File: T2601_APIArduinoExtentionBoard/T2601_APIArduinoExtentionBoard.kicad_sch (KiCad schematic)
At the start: 93 parts, among them J1 Conn_01x10_Socket, J11 Conn_01x04_Pin, J12 Screw_Terminal_01x02, J13 Conn_01x04_Pin, J14 Screw_Terminal_01x02, J15 Conn_02x08_Counter_Clockwise, J2 Conn_01x10_Socket, J3 Conn_01x10_Socket, J4 Conn_01x10_Socket, J5 Screw_Terminal_01x08, J6 Screw_Terminal_01x08, J7 Conn_02x03_Counter_Clockwise, J8 Conn_01x04, J9 Conn_02x08_Counter_Clockwise, U1 ATMEGA328P-AU, X1 X322516MOB4SI

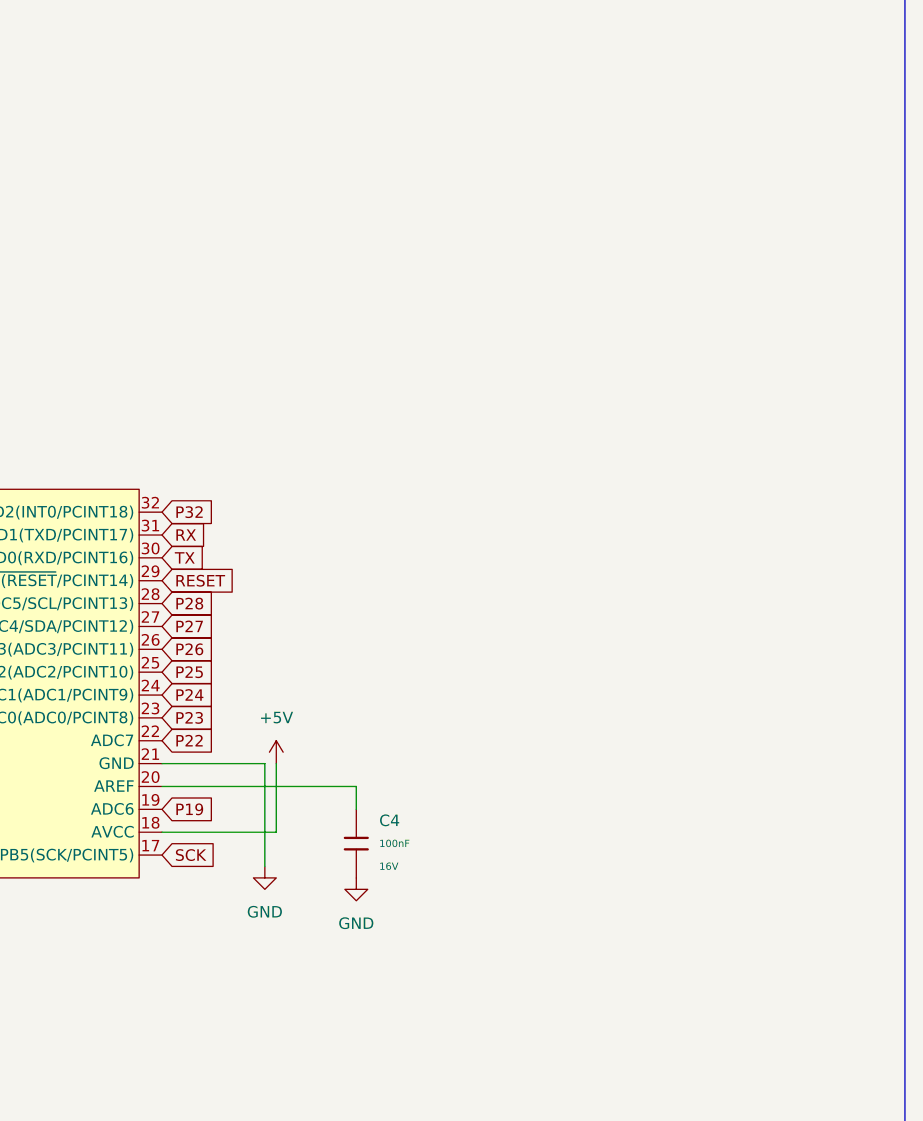
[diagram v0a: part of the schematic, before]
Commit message: switch to atmega328PB
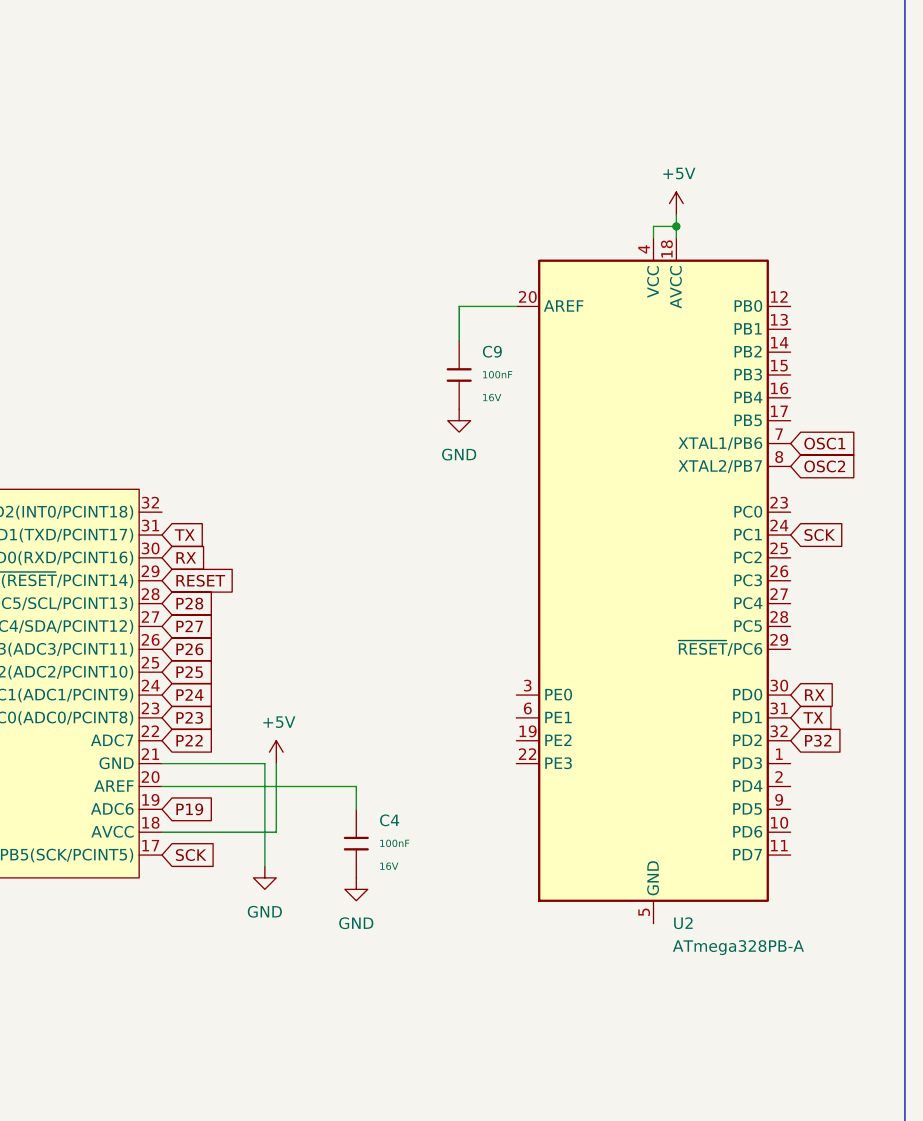
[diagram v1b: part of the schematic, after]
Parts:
- added C9: 100nF, PCM_JLCPCB:C_0402, symbol PCM_JLCPCB-Capacitors:0402,100nF
- added U2: ATmega328PB-A, Package_QFP:TQFP-32_7x7mm_P0.8mm, symbol MCU_Microchip_ATmega:ATmega328PB-A
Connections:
- net +5V: now also U2.18 (AVCC), U2.4 (VCC)
- net GND: now also C9.2
- net OSC1: now also U2.7 (XTAL1/PB6)
- net OSC2: now also U2.8 (XTAL2/PB7)
- net P32: now also U2.32 (PD2); no longer U1.32 (PD2(INT0/PCINT18))
- net RX: now also U1.30 (PD0(RXD/PCINT16)), U2.30 (PD0); no longer U1.31 (PD1(TXD/PCINT17))
- net SCK: now also U2.24 (PC1)
- net TX: now also U1.31 (PD1(TXD/PCINT17)), U2.31 (PD1); no longer U1.30 (PD0(RXD/PCINT16))
- new net: C9.1, U2.20 (AREF)
- new net: U2.21 (GND), U2.5 (GND)

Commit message: kicad modif
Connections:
- net MISO: now also U2.23 (PC0)
- net MOSI: now also U2.22 (PE3)
- net P1: now also U2.1 (PD3)
- net P2: now also U2.2 (PD4)
- net RESET: now also U2.29 (~{RESET}/PC6); no longer U1.29 (~{PC6(RESET}/PCINT14))
- net RX: no longer U1.30 (PD0(RXD/PCINT16))
- net TX: no longer U1.31 (PD1(TXD/PCINT17))
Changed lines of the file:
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@@
+		)
+	)
+	(global_label "P25"
+		(shape input)
+		(at 365.76 294.64 0)
+		(fields_autoplaced yes)
+		(effects
+			(font
+				(size 1.27 1.27)
+			)
+			(justify left)
+		)
+		(property "Intersheetrefs" "${INTERSHEET_REFS}"
+			(at 372.4342 294.64 0)
+			(hide yes)
+			(show_name no)
+			(do_not_autoplace no)
+			(effects
+				(font
+					(size 1.27 1.27)
+				)
+				(justify left)
+			)
 		)
 	)
@@
 		)
 	)
+	(global_label "MOSI"
+		(shape input)
+		(at 306.07 317.5 180)
+		(fields_autoplaced yes)
+		(effects
+			(font
+				(size 1.27 1.27)
+			)
+			(justify right)
+		)
+		(property "Intersheetrefs" "${INTERSHEET_REFS}"
+			(at 298.4886 317.5 0)
+			(hide yes)
+			(show_name no)
+			(do_not_autoplace no)
+			(effects
+				(font
+					(size 1.27 1.27)
+				)
+				(justify right)
+			)
+		)
+	)
 	(global_label "P12"
 		(shape input)
@@
 		)
 	)
+	(global_label "P27"
+		(shape input)
+		(at 365.76 299.72 0)
+		(fields_autoplaced yes)
+		(effects
+			(font
+				(size 1.27 1.27)
+			)
+			(justify left)
+		)
+		(property "Intersheetrefs" "${INTERSHEET_REFS}"
+			(at 372.4342 299.72 0)
+			(hide yes)
+			(show_name no)
+			(do_not_autoplace no)
+			(effects
+				(font
+					(size 1.27 1.27)
+				)
+				(justify left)
+			)
+		)
+	)
 	(global_label "TX_DEBUG"
 		(shape input)
@@
 	(global_label "RESET"
 		(shape input)
-		(at 266.7 297.18 0)
-		(fields_autoplaced yes)
-		(effects
-			(font
-				(size 1.27 1.27)
-			)
-			(justify left)
-		)
-		(property "Intersheetrefs" "${INTERSHEET_REFS}"
-			(at 275.4303 297.18 0)
+		(at 336.55 304.8 0)
+		(fields_autoplaced yes)
+		(effects
+			(font
+				(size 1.27 1.27)
+			)
+			(justify left)
+		)
+		(property "Intersheetrefs" "${INTERSHEET_REFS}"
+			(at 345.2803 304.8 0)
 			(hide yes)
 			(show_name no)
@@
 		)
 	)
+	(global_label "MISO"
+		(shape input)
+		(at 336.55 289.56 0)
+		(fields_autoplaced yes)
+		(effects
+			(font
+				(size 1.27 1.27)
+			)
+			(justify left)
+		)
+		(property "Intersheetrefs" "${INTERSHEET_REFS}"
+			(at 344.1314 289.56 0)
+			(hide yes)
+			(show_name no)
+			(do_not_autoplace no)
+			(effects
+				(font
+					(size 1.27 1.27)
+				)
+				(justify left)
+			)
+		)
+	)
 	(global_label "P1"
 		(shape input)
@@
 		)
 	)
+	(global_label "P1"
+		(shape input)
+		(at 336.55 317.5 0)
+		(fields_autoplaced yes)
+		(effects
+			(font
+				(size 1.27 1.27)
+			)
+			(justify left)
+		)
+		(property "Intersheetrefs" "${INTERSHEET_REFS}"
+			(at 342.0147 317.5 0)
+			(hide yes)
+			(show_name no)
+			(do_not_autoplace no)
+			(effects
+				(font
+					(size 1.27 1.27)
+				)
+				(justify left)
+			)
+		)
+	)
 	(global_label "P13"
 		(shape input)
@@
 		)
 	)
+	(global_label "P2"
+		(shape input)
+		(at 336.55 320.04 0)
+		(fields_autoplaced yes)
+		(effects
+			(font
+				(size 1.27 1.27)
+			)
+			(justify left)
+		)
+		(property "Intersheetrefs" "${INTERSHEET_REFS}"
+			(at 342.0147 320.04 0)
+			(hide yes)
+			(show_name no)
+			(do_not_autoplace no)
+			(effects
+				(font
+					(size 1.27 1.27)
+				)
+				(justify left)
+			)
+		)
+	)
+	(global_label "P28"
+		(shape input)
+		(at 365.76 302.26 0)
+		(fields_autoplaced yes)
+		(effects
+			(font
+				(size 1.27 1.27)
+			)
+			(justify left)
+		)
+		(property "Intersheetrefs" "${INTERSHEET_REFS}"
+			(at 372.4342 302.26 0)
+			(hide yes)
+			(show_name no)
+			(do_not_autoplace no)
+			(effects
+				(font
+					(size 1.27 1.27)
+				)
+				(justify left)
+			)
+		)
+	)
 	(global_label "P14"
 		(shape input)
@@
 		)
 	)
-	(global_label "TX"
-		(shape input)
-		(at 266.7 292.1 0)
-		(fields_autoplaced yes)
-		(effects
-			(font
-				(size 1.27 1.27)
-			)
-			(justify left)
-		)
-		(property "Intersheetrefs" "${INTERSHEET_REFS}"
-			(at 271.8623 292.1 0)
-			(hide yes)
-			(show_name no)
-			(do_not_autoplace no)
-			(effects
-				(font
-					(size 1.27 1.27)
-				)
-				(justify left)
-			)
-		)
-	)
 	(global_label "P11"
 		(shape input)
@@
 		)
 	)
+	(global_label "P26"
+		(shape input)
+		(at 365.76 297.18 0)
+		(fields_autoplaced yes)
+		(effects
+			(font
+				(size 1.27 1.27)
+			)
+			(justify left)
+		)
+		(property "Intersheetrefs" "${INTERSHEET_REFS}"
+			(at 372.4342 297.18 0)
+			(hide yes)
+			(show_name no)
+			(do_not_autoplace no)
+			(effects
+				(font
+					(size 1.27 1.27)
+				)
+				(justify left)
+			)
+		)
+	)
 	(global_label "MISO"
 		(shape input)
@@
 			(hide yes)
 			(show_name no)
-			(do_not_autoplace no)
-			(effects
-				(font
-					(size 1.27 1.27)
-				)
-				(justify left)
-			)
-		)
-	)
-	(global_label "RX"
-		(shape input)
-		(at 266.7 294.64 0)
-		(fields_autoplaced yes)
-		(effects
-			(font
-				(size 1.27 1.27)
-			)
-			(justify left)
-		)
-		(property "Intersheetrefs" "${INTERSHEET_REFS}"
-			(at 272.1647 294.64 0)
-			(hide yes)
-			(show_name no)

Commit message: Kicad Modification, switch ATMEGA328P to ATMEGA328PB, schematic modification + rerouting, V0 version, no verification
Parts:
- removed C4: 100nF, PCM_JLCPCB:C_0402, symbol PCM_JLCPCB-Capacitors:0402,100nF
- removed D13: Red, PCM_JLCPCB:D_0805, symbol PCM_JLCPCB-Diodes:LED,0805,Red
- removed R2: 1kΩ, PCM_JLCPCB:R_0402, symbol PCM_JLCPCB-Resistors:0402,1kΩ
- removed U1: ATMEGA328P-AU, T2601_APIArduinoExtentionBoard_Lib:TQFP-32_L7.0-W7.0-P0.80-LS9.0-BL, symbol T2601_APIArduinoExtentionBoard_Lib:ATMEGA328P-AU
- added D27: Red, PCM_JLCPCB:D_0805, symbol PCM_JLCPCB-Diodes:LED,0805,Red
- added D28: Green, PCM_JLCPCB:D_0805, symbol PCM_JLCPCB-Diodes:LED,0805,Green
- added D29: Yellow, PCM_JLCPCB:D_0805, symbol PCM_JLCPCB-Diodes:LED,0805,Yellow
- added R26, R27, R28: 1kΩ, PCM_JLCPCB:R_0402, symbol PCM_JLCPCB-Resistors:0402,1kΩ
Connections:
- net GND: now also U2.21 (GND), U2.5 (GND), R26.2, R27.2, R28.2
- net MISO: now also U2.16 (PB4); no longer U2.23 (PC0)
- net MOSI: now also U2.15 (PB3); no longer U2.22 (PE3)
- net P10: now also J4.8 (Pin_8), R9.1, U2.10 (PD6); no longer J4.7 (Pin_7), R10.1
- net P11: now also J4.7 (Pin_7), R10.1, U2.11 (PD7); no longer J4.4 (Pin_4), R11.1
- net P12: now also J4.4 (Pin_4), R11.1, U2.12 (PB0); no longer J4.3 (Pin_3), R12.1
- net P13: now also J4.3 (Pin_3), R12.1, U2.13 (PB1); no longer J4.2 (Pin_2), R13.1
- net P14: now also J4.2 (Pin_2), R13.1, U2.14 (PB2); no longer J4.1 (Pin_1), R14.1
- net P19: now also U2.19 (PE2)
- net P2: now also J8.2 (Pin_2), D27.2; no longer J4.9 (Pin_9), R8.1
- net P22: now also U2.22 (PE3)
- net P23: now also U2.23 (PC0)
- net P24: now also U2.24 (PC1)
- net P25: now also U2.25 (PC2)
- net P26: now also U2.26 (PC3)
- net P27: now also U2.27 (PC4)
- net P28: now also U2.28 (PC5)
- net P32: now also J4.1 (Pin_1), R14.1; no longer J8.2 (Pin_2)
- net P9: now also J4.9 (Pin_9), R8.1, U2.9 (PD5); no longer J4.8 (Pin_8), R9.1
- net SCK: now also U2.17 (PB5); no longer U2.24 (PC1)
- net P3: now reaches U2.3 (PE0)
- net P3: now also D28.2
- net P6: now reaches U2.6 (PE1)
- net P6: now also D29.2
- new net: D29.1, R28.1
- new net: D28.1, R27.1
- new net: D27.1, R26.1
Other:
- note added: "State Indicator"
- note removed: "BLINK Indicator"
- moved on the sheet: C5, C6, C9, H1, H2, H3, H4, TP1, U2

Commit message: Modification Board to 4 layers, finition routing et re organisation des composants (leds statuts condo alim + reset
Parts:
- added TP2: TestPoint, TestPoint:TestPoint_Loop_D2.50mm_Drill1.0mm_LowProfile, symbol Connector:TestPoint
- TP1: footprint TestPoint:TestPoint_Pad_D2.0mm -> TestPoint:TestPoint_Loop_D2.50mm_Drill1.0mm_LowProfile
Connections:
- net RX: now also D12.2, TP2.1; no longer D11.2
- net TX: now also D11.2; no longer D12.2
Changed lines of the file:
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@@
 	(wire
 		(pts
+			(xy 39.37 190.5) (xy 38.1 190.5)
+		)
+		(stroke
+			(width 0)
+			(type default)
+		)
+	)
+	(wire
+		(pts
 			(xy 256.54 116.84) (xy 261.62 116.84)
 		)
@@
 	(wire
 		(pts
+			(xy 38.1 190.5) (xy 38.1 186.69)
+		)
+		(stroke
+			(width 0)
+			(type default)
+		)
+	)
+	(wire
+		(pts
 			(xy 262.89 41.91) (xy 262.89 40.64)
 		)
@@
 	(global_label "RX"
 		(shape input)
-		(at 24.13 69.85 90)
+		(at 34.29 69.85 90)
 		(fields_autoplaced yes)
 		(effects
@@
 		)
 		(property "Intersheetrefs" "${INTERSHEET_REFS}"
-			(at 24.13 64.3853 90)
+			(at 34.29 64.3853 90)
 			(hide yes)
 			(show_name no)
@@
 	(global_label "TX"
 		(shape input)
-		(at 34.29 69.85 90)
+		(at 24.13 69.85 90)
 		(fields_autoplaced yes)
 		(effects
@@
 		)
 		(property "Intersheetrefs" "${INTERSHEET_REFS}"
-			(at 34.29 64.6877 90)
+			(at 24.13 64.6877 90)
 			(hide yes)
 			(show_name no)
@@
 		)
 	)
+	(global_label "RX"
+		(shape input)
+		(at 39.37 190.5 0)
+		(fields_autoplaced yes)
+		(effects
+			(font
+				(size 1.27 1.27)
+			)
+			(justify left)
+		)
+		(property "Intersheetrefs" "${INTERSHEET_REFS}"
+			(at 44.8347 190.5 0)
+			(hide yes)
+			(show_name no)
+			(do_not_autoplace no)
+			(effects
+				(font
+					(size 1.27 1.27)
+				)
+				(justify left)
+			)
+		)
+	)
 	(global_label "P1"
 		(shape input)
@@
 	)
 	(symbol
+		(lib_id "Connector:TestPoint")
+		(at 38.1 186.69 0)
+		(unit 1)
+		(body_style 1)
+		(exclude_from_sim no)
+		(in_bom yes)
+		(on_board yes)
+		(in_pos_files yes)
+		(dnp no)
+		(fields_autoplaced yes)
+		(property "Reference" "TP2"
+			(at 40.64 182.1179 0)
+			(show_name no)
+			(do_not_autoplace no)
+			(effects
+				(font
+					(size 1.27 1.27)
+				)
+				(justify left)
+			)
+		)
+		(property "Value" "TestPoint"
+			(at 40.64 184.6579 0)
+			(show_name no)
+			(do_not_autoplace no)
+			(effects
+				(font
+					(size 1.27 1.27)
+				)
+				(justify left)
+			)
+		)
+		(property "Footprint" "TestPoint:TestPoint_Loop_D2.50mm_Drill1.0mm_LowProfile"
+			(at 43.18 186.69 0)
+			(show_name no)
+			(do_not_autoplace no)
+			(effects
+				(font
+					(size 1.27 1.27)
+				)
+			)
+		)
+		(property "Datasheet" ""
+			(at 43.18 186.69 0)
+			(hide yes)
+			(show_name no)
+			(do_not_autoplace no)
+			(effects
+				(font
+					(size 1.27 1.27)
+				)
+			)
+		)
+		(property "Description" "test point"
+			(at 38.1 186.69 0)
+			(hide yes)
+			(show_name no)
+			(do_not_autoplace no)
+			(effects
+				(font
+					(size 1.27 1.27)
+				)
+			)
+		)
+		(pin "1"
+		)
+		(instances
+			(project "T2601_APIArduinoExtentionBoard"
+				(path "/ff48760a-7750-46de-b467-7e55c22e4653"
+					(reference "TP2")
+					(unit 1)
+				)
+			)
+		)
+	)
+	(symbol
 		(lib_id "power:GND")
 		(at 149.86 365.76 0)
@@
 			)
 		)
-		(property "Footprint" "TestPoint:TestPoint_Pad_D2.0mm"
+		(property "Footprint" "TestPoint:TestPoint_Loop_D2.50mm_Drill1.0mm_LowProfile"
 			(at 62.23 132.08 0)
-			(hide yes)
 			(show_name no)
 			(do_not_autoplace no)

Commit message: Resolution de diversse ISSUE, position UART, Rerouting, modif VIA
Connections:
- net RX: no longer TP2.1
- net TX: now also TP2.1
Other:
- moved on the sheet: TP1
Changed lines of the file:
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@@
 	(wire
 		(pts
-			(xy 58.42 135.89) (xy 57.15 135.89)
+			(xy 104.14 190.5) (xy 102.87 190.5)
 		)
 		(stroke
@@
 	(wire
 		(pts
-			(xy 57.15 135.89) (xy 57.15 132.08)
+			(xy 102.87 190.5) (xy 102.87 186.69)
 		)
 		(stroke
@@
 		)
 	)
+	(global_label "TX"
+		(shape input)
+		(at 39.37 190.5 0)
+		(fields_autoplaced yes)
+		(effects
+			(font
+				(size 1.27 1.27)
+			)
+			(justify left)
+		)
+		(property "Intersheetrefs" "${INTERSHEET_REFS}"
+			(at 44.5323 190.5 0)
+			(hide yes)
+			(show_name no)
+			(do_not_autoplace no)
+			(effects
+				(font
+					(size 1.27 1.27)
+				)
+				(justify left)
+			)
+		)
+	)
 	(global_label "P27"
 		(shape input)
@@
 	(global_label "UART_BACK"
 		(shape input)
-		(at 58.42 135.89 0)
+		(at 104.14 190.5 0)
 		(fields_autoplaced yes)
 		(effects
@@
 		)
 		(property "Intersheetrefs" "${INTERSHEET_REFS}"
-			(at 71.9281 135.89 0)
+			(at 117.6481 190.5 0)
 			(hide yes)
 			(show_name no)
@@
 		)
 	)
-	(global_label "RX"
-		(shape input)
-		(at 39.37 190.5 0)
-		(fields_autoplaced yes)
-		(effects
-			(font
-				(size 1.27 1.27)
-			)
-			(justify left)
-		)
-		(property "Intersheetrefs" "${INTERSHEET_REFS}"
-			(at 44.8347 190.5 0)
-			(hide yes)
-			(show_name no)
-			(do_not_autoplace no)
-			(effects
-				(font
-					(size 1.27 1.27)
-				)
-				(justify left)
-			)
-		)
-	)
 	(global_label "P1"
 		(shape input)
@@
 	(symbol
 		(lib_id "Connector:TestPoint")
-		(at 57.15 132.08 0)
+		(at 102.87 186.69 0)
 		(unit 1)
 		(body_style 1)
@@
 		(fields_autoplaced yes)
 		(property "Reference" "TP1"
-			(at 59.69 127.5079 0)
+			(at 105.41 182.1179 0)
 			(show_name no)
 			(do_not_autoplace no)
@@
 		)
 		(property "Value" "TestPoint"
-			(at 59.69 130.0479 0)
+			(at 105.41 184.6579 0)
 			(show_name no)
 			(do_not_autoplace no)
@@
 		)
 		(property "Footprint" "TestPoint:TestPoint_Loop_D2.50mm_Drill1.0mm_LowProfile"
-			(at 62.23 132.08 0)
+			(at 107.95 186.69 0)
 			(show_name no)
 			(do_not_autoplace no)
@@
 		)
 		(property "Datasheet" ""
-			(at 62.23 132.08 0)
+			(at 107.95 186.69 0)
 			(hide yes)
 			(show_name no)
@@
 		)
 		(property "Description" "test point"
-			(at 57.15 132.08 0)
+			(at 102.87 186.69 0)
 			(hide yes)
 			(show_name no)

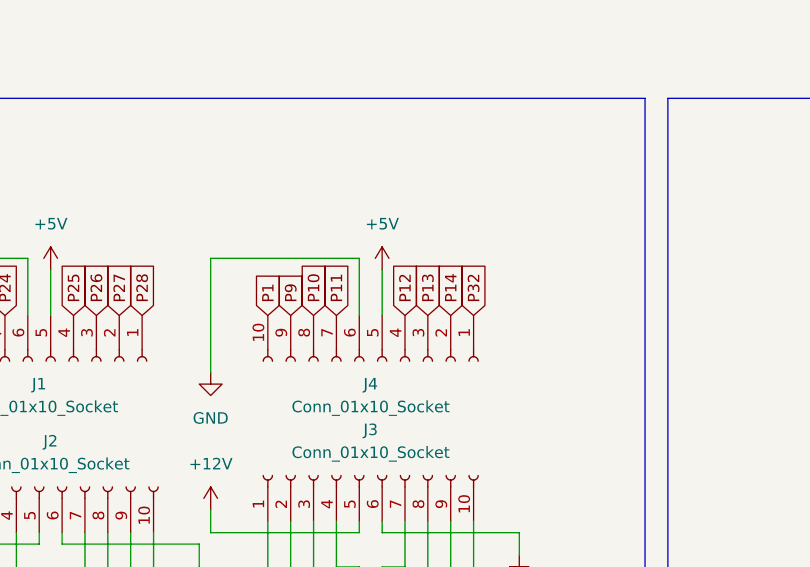
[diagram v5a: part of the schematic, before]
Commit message: Modification affectation pin PWM Mezz 1
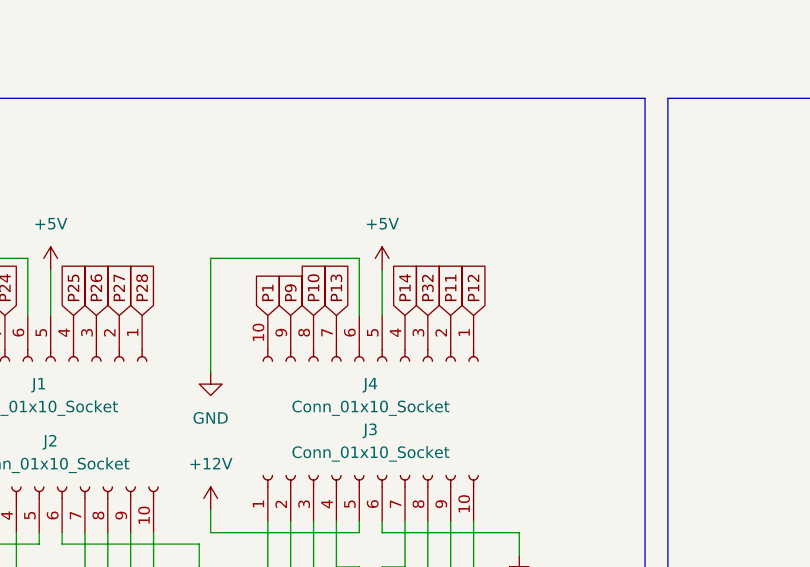
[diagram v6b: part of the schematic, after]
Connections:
- net P11: now also J4.2 (Pin_2); no longer J4.7 (Pin_7)
- net P12: now also J4.1 (Pin_1); no longer J4.4 (Pin_4)
- net P13: now also J4.7 (Pin_7); no longer J4.3 (Pin_3)
- net P14: now also J4.4 (Pin_4); no longer J4.2 (Pin_2)
- net P32: now also J4.3 (Pin_3); no longer J4.1 (Pin_1)
